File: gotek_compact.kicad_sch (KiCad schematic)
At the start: 32 parts, among them IC1 STM32F105RBT6, IC2 74AHCT08D, IC3 AP7381-33Y-13, X1 8MHz

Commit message: Updated Schematics and initial PCB placement
Schematics have been re-done based on OpenFlop from SukkoPera, with changes towards more compact design.
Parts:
- removed IC1: STM32F105RBT6, Package_QFP:LQFP-64_10x10mm_P0.5mm, symbol MCU_ST_STM32F1:STM32F105RBTx
- removed IC2: 74AHCT08D, Package_SO:SOIC-14_3.9x8.7mm_P1.27mm, symbol 74xx:74LS08
- removed IC3: AP7381-33Y-13, Package_TO_SOT_SMD:SOT-89-3, symbol Regulator_Linear:AP7381-33V
- removed LK1: BOOT0, Connector_PinHeader_2.54mm:PinHeader_1x02_P2.54mm_Vertical, symbol Connector_Generic:Conn_01x02
- removed PL1: Power 5V, Connector_PinHeader_2.54mm:PinHeader_1x02_P2.54mm_Vertical, symbol Connector_Generic:Conn_01x02
- removed PL2: Program, Connector_PinHeader_2.54mm:PinHeader_1x03_P2.54mm_Vertical, symbol Connector_Generic:Conn_01x03
- removed PL3: USB, Connector_PinHeader_2.54mm:PinHeader_1x04_P2.54mm_Vertical, symbol Connector_Generic:Conn_01x04
- removed PL5: OLED, Connector_PinHeader_2.54mm:PinHeader_1x04_P2.54mm_Vertical, symbol Connector_Generic:Conn_01x04
- removed VR1: 10K, Potentiometer_SMD:Potentiometer_Bourns_TC33X_Vertical, symbol Device:R_Potentiometer_Trim
- added C10: 100nF, Capacitor_SMD:C_0805_2012Metric, symbol Device:C
- added C11, C12: 22pF, Capacitor_SMD:C_0805_2012Metric, symbol Device:C
- added CN1: POWER_IN, gotek_compact:171826-4, symbol gotek_compact:171826-4
- added CN2: USB, gotek_compact:USB-C-SMD_GT-USB-7016, symbol gotek_compact:GT-USB-7016
- added D1: 1N4148WS, Diode_SMD:D_SOD-323, symbol Diode:1N4148WS
- added J2: USB_Prog, Connector_PinHeader_2.54mm:PinHeader_2x05_P2.54mm_Vertical, symbol Connector_Generic:Conn_02x05_Odd_Even
- added J3: OLED+SER, Connector_PinHeader_2.54mm:PinHeader_1x06_P2.54mm_Vertical, symbol Connector_Generic:Conn_01x06
- added Q1: MMBT3904, Package_TO_SOT_SMD:SOT-23, symbol Transistor_BJT:MMBT3904
- added R12: 22, Resistor_SMD:R_0805_2012Metric, symbol Device:R
- added R13: 1K, Resistor_SMD:R_0805_2012Metric, symbol Device:R
- added R14, R15: 5K1, Resistor_SMD:R_0805_2012Metric, symbol Device:R
- added R5: 4K7, Resistor_SMD:R_0805_2012Metric, symbol Device:R
- added U1: STM32F105RBT6, Package_QFP:LQFP-64_10x10mm_P0.5mm, symbol MCU_ST_STM32F1:STM32F105RBTx
- added U2: 74LCX07, Package_SO:TSSOP-14_4.4x5mm_P0.65mm, symbol 74xx:74LCX07
- added U3: AP2112K-3.3, Package_TO_SOT_SMD:SOT-23-5, symbol Regulator_Linear:AP2112K-1.2
- C1: value 10uF/16V -> 1uF; footprint Capacitor_SMD:C_1206_3216Metric -> Capacitor_SMD:C_0805_2012Metric; LCSC (none) -> C28323; Part Number (none) -> CL21B105KBFNNNE
- C2: value 100nF -> 10uF; LCSC (none) -> C15850; Part Number (none) -> CL21A106KAYNNNE
- C3: value 2u2 -> 10uF; LCSC (none) -> C15850; Part Number (none) -> CL21A106KAYNNNE
- C4, C5, C8, C9: LCSC (none) -> C49678; Part Number (none) -> CC0805KRX7R9BB104
- C6, C7: value 22pF -> 100nF; LCSC (none) -> C49678; Part Number (none) -> CC0805KRX7R9BB104
- CN3: renamed from SK1; LCSC (none) -> C601943; Part Number (none) -> 321034SG0ABK00A01
- J1: renamed from PL4; LCSC (none) -> C5383111; Part Number (none) -> 2541WV-02P
- J4: renamed from PL6; LCSC (none) -> C5383114; Part Number (none) -> 2541WV-05P
- R1, R4: LCSC (none) -> C17673; Part Number (none) -> 0805W8F4701T5E
- R10, R11, R6, R7, R8, R9: value 1K0 -> 1K; LCSC (none) -> C17513; Part Number (none) -> 0805W8F1001T5E
- R2, R3: LCSC (none) -> C17561; Part Number (none) -> 0805W8F220JT5E
- X1: footprint Crystal:Crystal_SMD_HC49-SD -> Crystal:Crystal_SMD_5032-2Pin_5.0x3.2mm; LCSC (none) -> X50328MSB2GI; Part Number (none) -> C115962
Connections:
- net SOUNDER is gone; now on net GND: R4.1
- net SOUND_POT is gone; now on net BOOT0: R4.2
- net +3V3: now also C2.1, C4.2, C5.2, C6.2, C7.2, C8.2, C9.2, R1.2, J2.10 (Pin_10), J2.7 (Pin_7), J3.4 (Pin_4), U1.1 (VBAT), U1.13 (VDDA), U1.19 (VDD), U1.32 (VDD), U1.48 (VDD), U1.64 (VDD), U2.14 (VCC), U3.5 (VOUT); no longer C4.1, C5.1, R1.1
- net +5V: now also R10.2, R11.2, R6.2, R7.2, R8.2, R9.2, CN1.1 (5V), CN2.A4B9 (VBUS), CN2.B4A9 (VBUS), J2.4 (Pin_4), R12.2, U3.1 (VIN), U3.3 (EN); no longer C2.1, C9.1, R10.1, R11.1, R6.1, R7.1, R8.1, R9.1
- net BOOT0: now also J2.9 (Pin_9), U1.60 (BOOT0)
- net ENC_CLK: now also U1.52 (PC11)
- net ENC_DT: now also U1.51 (PC10)
- net ENC_SW: now also U1.37 (PC6)
- net GND: now also C4.1, C5.1, C6.1, C7.1, C8.1, C9.1, C10.1, C11.2, C12.2, CN1.2 (GND), CN1.3 (GND), CN2.0 (SHELL), CN2.A1B12 (GND), CN2.B1A12 (GND), J2.2 (Pin_2), J2.6 (Pin_6), J2.8 (Pin_8), J3.3 (Pin_3), Q1.2 (E), R14.2, R15.2, R5.2, U1.12 (VSSA), U1.18 (VSS), U1.2 (PC13), U1.3 (PC14), U1.31 (VSS), U1.4 (PC15), U1.47 (VSS), U1.53 (PC12), U1.63 (VSS), U2.7 (GND), U3.2 (GND); no longer C4.2, C5.2, C6.2, C7.2, C8.2, C9.2, J1.2 (Pin_2)
- net NRST: now also R1.1, C10.2, J2.1 (Pin_1), U1.7 (NRST); no longer C8.1, R1.2
- net OSC_IN: now also C11.1, U1.5 (PD0); no longer C6.1
- net OSC_OUT: now also C12.1, U1.6 (PD1); no longer C7.1
- net RXD: now also J2.3 (Pin_3), U1.42 (PA9)
- net SCL: now also J3.5 (Pin_5), U1.29 (PB10)
- net SDA: now also J3.6 (Pin_6), U1.30 (PB11)
- net SOUND: now also R13.1, U1.16 (PA2); no longer J1.1 (Pin_1)
- net SWCLK: now also J3.1 (Pin_1), U1.49 (PA14)
- net SWDIO: now also J3.2 (Pin_2), U1.46 (PA13)
- net TXD: now also J2.5 (Pin_5), U1.43 (PA10)
- net _CHNG: now reaches CN3.2 (Pin_2)
- net _CHNG: now also U2.12
- net _RDY: now reaches CN3.34 (Pin_34)
- net _RDY: now also U2.10
- net DIRECTION renamed DIR
- net DIR: now also R11.1, U1.26 (PB0); no longer R11.2
- net DRIVE_SELECT_0 renamed _SEL0
- net _SEL0: now also R6.1, U1.14 (PA0); no longer R6.2
- net INDEX renamed _INDEX
- net _INDEX: now also U2.6
- net READ_DATA renamed _DKRD
- net _DKRD: now also U2.2
- net SIDE_SELECT renamed _SIDE
- net _SIDE: now also R10.1, U1.56 (PB4); no longer R10.2
- net STEP renamed _STEP
- net _STEP: now also R7.1, U1.15 (PA1); no longer R7.2
- net TRK0 renamed _TRK0
- net _TRK0: now also U2.4
- net USB_DM renamed USB_D-
- net USB_D-: now also CN2.A7 (DN1), CN2.B7 (DN2)
- net USB_DM_MCU: no longer names the net of R2.1
- net USB_DM_MCU: now also U1.44 (PA11)
- net USB_DP renamed USB_D+
- net USB_D+: now also CN2.A6 (DP1), CN2.B6 (DP2)
- net USB_DP_MCU: no longer names the net of R3.1
- net USB_DP_MCU: now also U1.45 (PA12)
- net WRITE_DATA renamed _DKWD
- net _DKWD: now also R8.1, U1.41 (PA8); no longer R8.2
- net WRITE_ENABLE renamed _DKWE
- net _DKWE: now also R9.1, U1.62 (PB9); no longer R9.2
- net WRITE_PROTECT renamed _WPROT
- net _WPROT: now also U2.8
- new net: R5.1, U1.28 (PB2)
- new net: D1.2 (A), Q1.3 (C)
- new net: Q1.1 (B), R13.2
- new net SPK+: J1.1 (Pin_1), R12.1
- new net SPK-: D1.1 (K), J1.2 (Pin_2)
- new net USB_CC1: CN2.A5 (CC1), R14.1
- new net USB_CC2: CN2.B5 (CC2), R15.1
- new net _CHNG_3V: U1.59 (PB7), U2.13
- new net _DKRD_3V: U1.23 (PA7), U2.1
- new net _INDEX_3V: U1.61 (PB8), U2.5
- new net _RDY_3V: U1.55 (PB3), U2.11
- new net _TRK0_3V: U1.58 (PB6), U2.3
- new net _WPROT_3V: U1.57 (PB5), U2.9
- no-connect marks 34 -> 28
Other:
- note added: "1K pull-ups on host-driven inputs"
- note added: "34-pin boxed IDC header (top side), standard floppy ribbon pinout"
- note added: "Open Drain Buffers to 5V TTL"
- note removed: "1K pull-ups (R6-R11) on host-driven inputs"
- note removed: "Buffers 3V3 MCU outputs to 5V TTL: Index, Track0, Write Protect, Read Data"
- note removed: "Compact Gotek core - circuit derived from CDO's Issue 1.1 design (theoddys.com) Gotek-compatible floppy emulator for the BBC Master internal 34-way floppy header. Programming: fit BOOT0 link LK1, connect 3V3 FTDI to PL2, use STM32CubeProgrammer; firmware: FlashFloppy. NOTE: Do not use with an external floppy drive connected at the same time (no open-collector drivers)."
- note removed: "PL1 -> 5V power in PL2 -> FTDI (3V3) programming PL3 -> USB-A breakout (stick) PL4 -> sound out PL5 -> 0.96in OLED (I2C) PL6 -> KY-040 style rotary encoder SK1 -> 34-pin boxed IDC, standard Shugart floppy bus"
- note removed: "SK1: 34-pin boxed IDC header (top side), standard floppy ribbon pinout"
- company: KiCad recreation of design by CDO / theoddys.com -> Derived from OpenFlops
- title: Compact Gotek / FlashFloppy core with breakout headers -> Compact Gotek / FlashFloppy with breakout headers
- moved on the sheet: CN3, J1, J4, X1

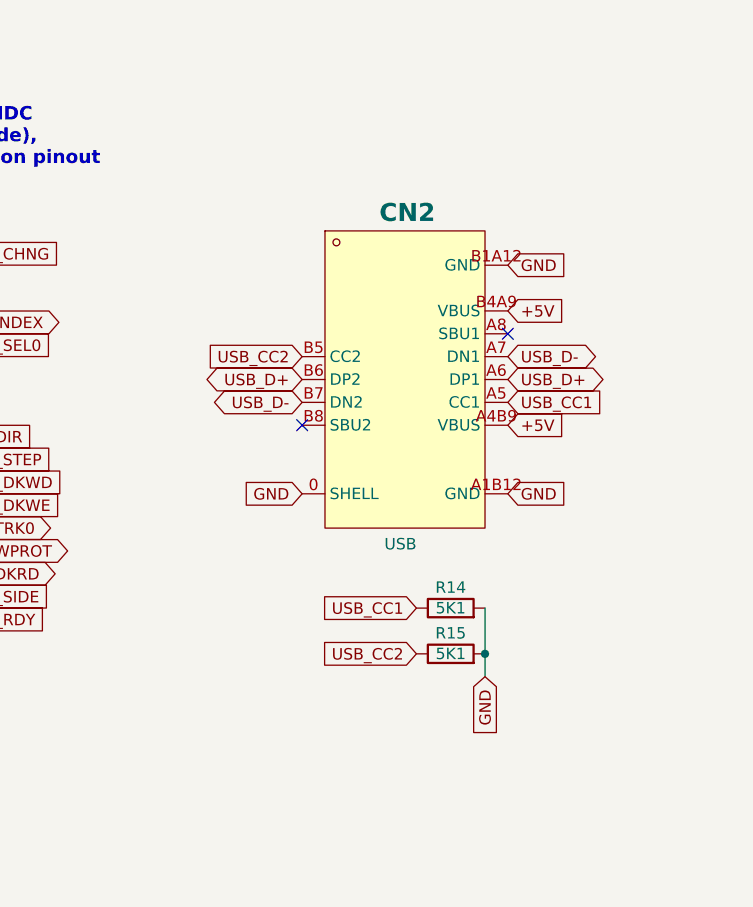
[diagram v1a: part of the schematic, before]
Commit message: USB connector changed
USB connector changed to a model without elevation
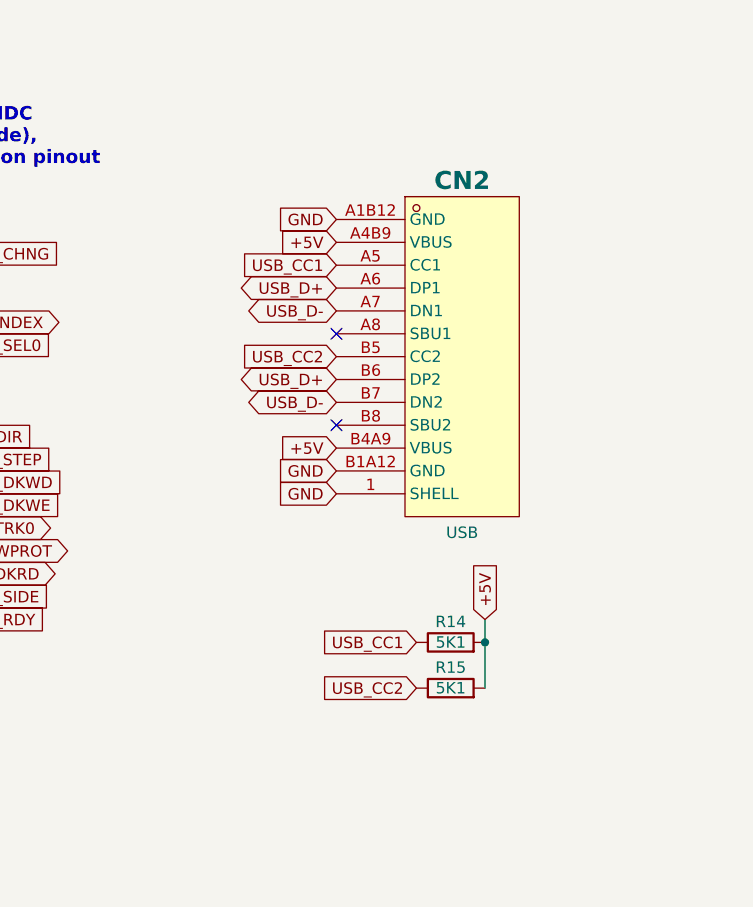
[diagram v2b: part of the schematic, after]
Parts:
- removed CN2: USB, gotek_compact:USB-C-SMD_GT-USB-7016, symbol gotek_compact:GT-USB-7016
- added CN2: USB, gotek_compact:USB-C-SMD_TYPE-C16PIN, symbol gotek_compact:TYPE-C16PIN
- U3: symbol Regulator_Linear:AP2112K-1.2 -> Regulator_Linear:AP2112K-3.3
- X1: LCSC X50328MSB2GI -> C115962; Part Number C115962 -> X50328MSB2GI
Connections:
- net +5V: now also R14.2, R15.2, CN2.A4B9 (VBUS), CN2.B4A9 (VBUS)
- net GND: now also CN2.1 (SHELL), CN2.2 (SHELL), CN2.3 (SHELL), CN2.4 (SHELL), CN2.A1B12 (GND), CN2.B1A12 (GND); no longer R14.2, R15.2
- net USB_CC1: now also CN2.A5 (CC1)
- net USB_CC2: now also CN2.B5 (CC2)
- net USB_D+: now also CN2.A6 (DP1), CN2.B6 (DP2)
- net USB_D-: now also CN2.A7 (DN1), CN2.B7 (DN2)
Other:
- moved on the sheet: R14, R15

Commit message: A few component value changes
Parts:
- C11, C12: value 22pF -> 30pF; footprint Capacitor_SMD:C_0805_2012Metric -> Capacitor_SMD:C_0603_1608Metric; LCSC C1804 -> C1658; Part Number CL21C220JBANNNC -> 0603CG300J500NT
- R14, R15: value 5K1 -> 51K; LCSC C27834 -> C17737; Part Number 0805W8F5101T5E -> 0805W8F5102T5E
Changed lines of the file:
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@@
 	)
 	(junction
+		(at 21.59 114.3)
+		(diameter 0)
+		(color 0 0 0 0)
+	)
+	(junction
 		(at 181.61 132.08)
 		(diameter 0)
@@
 	)
 	(junction
-		(at 21.59 114.3)
-		(diameter 0)
-		(color 0 0 0 0)
-	)
-	(junction
 		(at 35.56 114.3)
 		(diameter 0)
@@
 	(wire
 		(pts
+			(xy 21.59 114.3) (xy 21.59 118.11)
+		)
+		(stroke
+			(width 0)
+			(type default)
+		)
+	)
+	(wire
+		(pts
 			(xy 148.59 166.37) (xy 139.7 166.37)
 		)
@@
 	(wire
 		(pts
-			(xy 21.59 114.3) (xy 21.59 118.11)
+			(xy 21.59 105.41) (xy 21.59 114.3)
 		)
 		(stroke
@@
 	(wire
 		(pts
-			(xy 21.59 105.41) (xy 21.59 114.3)
-		)
-		(stroke
-			(width 0)
-			(type default)
-		)
-	)
-	(wire
-		(pts
 			(xy 181.61 127) (xy 181.61 129.54)
 		)
@@
 	)
 	(symbol
-		(lib_id "Device:C")
-		(at 25.4 114.3 270)
-		(unit 1)
-		(body_style 1)
-		(exclude_from_sim no)
-		(in_bom yes)
-		(on_board yes)
-		(in_pos_files yes)
-		(dnp no)
-		(property "Reference" "C12"
-			(at 26.924 113.284 90)
-			(show_name no)
-			(do_not_autoplace no)
-			(effects
-				(font
-					(size 1.27 1.27)
-				)
-				(justify left)
-			)
-		)
-		(property "Value" "22pF"
-			(at 26.924 115.824 90)
-			(show_name no)
-			(do_not_autoplace no)
-			(effects
-				(font
-					(size 1.27 1.27)
-				)
-				(justify left)
-			)
-		)
-		(property "Footprint" "Capacitor_SMD:C_0805_2012Metric"
-			(at 21.59 115.2652 0)
-			(hide yes)
-			(show_name no)
-			(do_not_autoplace no)
-			(effects
-				(font
-					(size 1.27 1.27)
-				)
-			)
-		)
-		(property "Datasheet" ""
-			(at 25.4 114.3 0)
-			(hide yes)
-			(show_name no)
-			(do_not_autoplace no)
-			(effects
-				(font
-					(size 1.27 1.27)
-				)
-			)
-		)
-		(property "Description" "Unpolarized capacitor"
-			(at 25.4 114.3 0)
-			(hide yes)
-			(show_name no)
-			(do_not_autoplace no)
-			(effects
-				(font
-					(size 1.27 1.27)
-				)
-			)
-		)
-		(property "LCSC" "C1804"
-			(at 25.4 114.3 0)
-			(hide yes)
-			(show_name no)
-			(do_not_autoplace no)
-			(effects
-				(font
-					(size 1.27 1.27)
-				)
-			)
-		)
-		(property "Part Number" "CL21C220JBANNNC"
-			(at 25.4 114.3 0)
-			(hide yes)
-			(show_name no)
-			(do_not_autoplace no)
-			(effects
-				(font
-					(size 1.27 1.27)
-				)
-			)
-		)
-		(pin "1"
-		)
-		(pin "2"
-		)
-		(instances
-			(project "gotek_compact"
-				(path "/e63e39d7-6ac0-4ffd-8aa3-1841a4541b55"
-					(reference "C12")
-					(unit 1)
-				)
-			)
-		)
-	)
-	(symbol
 		(lib_id "Device:R")
 		(at 248.92 152.4 90)
@@
 			)
 		)
-		(property "Value" "5K1"
+		(property "Value" "51K"
 			(at 248.92 152.4 90)
 			(show_name no)
@@
 			)
 		)
-		(property "LCSC" "C27834"
+		(property "LCSC" "C17737"
 			(at 248.92 152.4 90)
 			(hide yes)
@@
 			)
 		)
-		(property "Part Number" "0805W8F5101T5E"
+		(property "Part Number" "0805W8F5102T5E"
 			(at 248.92 152.4 90)
 			(hide yes)
@@
 			)
 		)
-		(property "Value" "22pF"
+		(property "Value" "30pF"
 			(at 27.178 106.934 90)
 			(show_name no)
@@
 			)
 		)
-		(property "Footprint" "Capacitor_SMD:C_0805_2012Metric"
+		(property "Footprint" "Capacitor_SMD:C_0603_1608Metric"
 			(at 21.59 106.3752 0)
 			(hide yes)
@@
 			)
 		)
-		(property "LCSC" "C1804"
+		(property "LCSC" "C1658"
 			(at 25.4 105.41 0)
 			(hide yes)
@@
 			)
 		)
-		(property "Part Number" "CL21C220JBANNNC"
+		(property "Part Number" "0603CG300J500NT"
 			(at 25.4 105.41 0)
 			(hide yes)
@@
 	)
 	(symbol
+		(lib_id "Device:C")
+		(at 25.4 114.3 270)
+		(unit 1)
+		(body_style 1)
+		(exclude_from_sim no)
+		(in_bom yes)
+		(on_board yes)
+		(in_pos_files yes)
+		(dnp no)
+		(property "Reference" "C12"
+			(at 26.924 113.284 90)
+			(show_name no)
+			(do_not_autoplace no)
+			(effects
+				(font
+					(size 1.27 1.27)
+				)
+				(justify left)
+			)
+		)
+		(property "Value" "30pF"
+			(at 27.178 115.824 90)
+			(show_name no)
+			(do_not_autoplace no)
+			(effects
+				(font
+					(size 1.27 1.27)
+				)
+				(justify left)
+			)
+		)
+		(property "Footprint" "Capacitor_SMD:C_0603_1608Metric"
+			(at 21.59 115.2652 0)
+			(hide yes)
+			(show_name no)
+			(do_not_autoplace no)
+			(effects
+				(font
+					(size 1.27 1.27)
+				)
+			)
+		)
+		(property "Datasheet" ""
+			(at 25.4 114.3 0)
+			(hide yes)
+			(show_name no)
+			(do_not_autoplace no)
+			(effects
+				(font
+					(size 1.27 1.27)
+				)
+			)
+		)
+		(property "Description" "Unpolarized capacitor"
+			(at 25.4 114.3 0)
+			(hide yes)
+			(show_name no)
+			(do_not_autoplace no)
+			(effects
+				(font
+					(size 1.27 1.27)
+				)
+			)
+		)
+		(property "LCSC" "C1658"
+			(at 25.4 114.3 0)
+			(hide yes)
+			(show_name no)
+			(do_not_autoplace no)
+			(effects
+				(font
+					(size 1.27 1.27)
+				)
+			)
+		)
+		(property "Part Number" "0603CG300J500NT"
+			(at 25.4 114.3 0)
+			(hide yes)
+			(show_name no)
+			(do_not_autoplace no)
+			(effects
+				(font
+					(size 1.27 1.27)
+				)
+			)
+		)
+		(pin "1"
+		)
+		(pin "2"
+		)
+		(instances
+			(project "gotek_compact"
+				(path "/e63e39d7-6ac0-4ffd-8aa3-1841a4541b55"
+					(reference "C12")
+					(unit 1)
+				)
+			)
+		)
+	)
+	(symbol
 		(lib_id "74xx:74LCX07")
 		(at 139.7 104.14 0)
@@
 			)
 		)
-		(property "Value" "5K1"
+		(property "Value" "51K"
 			(at 248.92 147.32 90)
 			(show_name no)
@@
 			)
 		)
-		(property "LCSC" "C27834"
+		(property "LCSC" "C17737"
 			(at 248.92 147.32 90)
 			(hide yes)
@@
 			)
 		)
-		(property "Part Number" "0805W8F5101T5E"
+		(property "Part Number" "0805W8F5102T5E"
 			(at 248.92 147.32 90)
 			(hide yes)

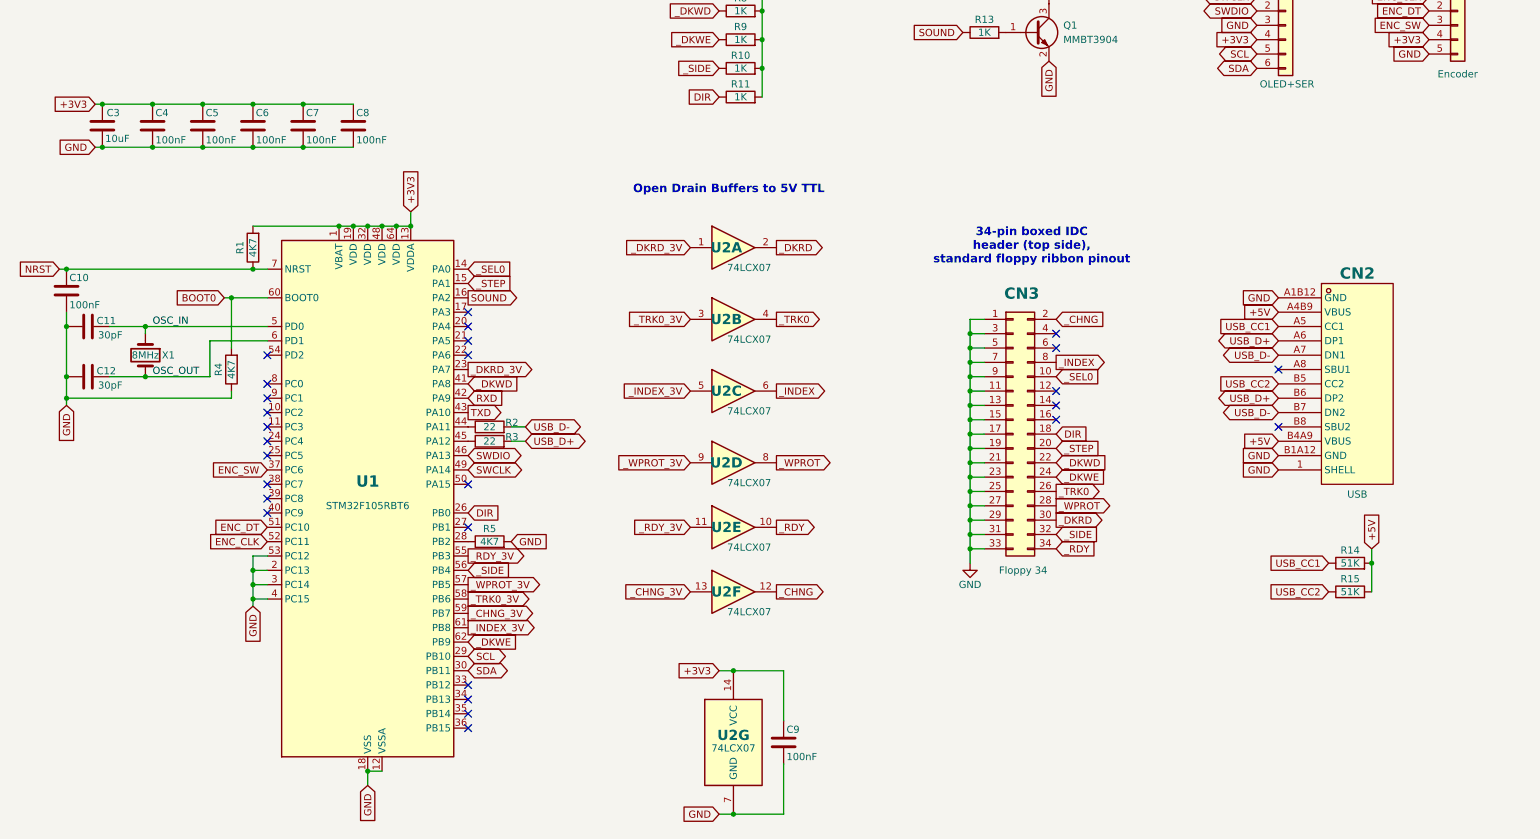
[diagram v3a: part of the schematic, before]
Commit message: PCB routing finished
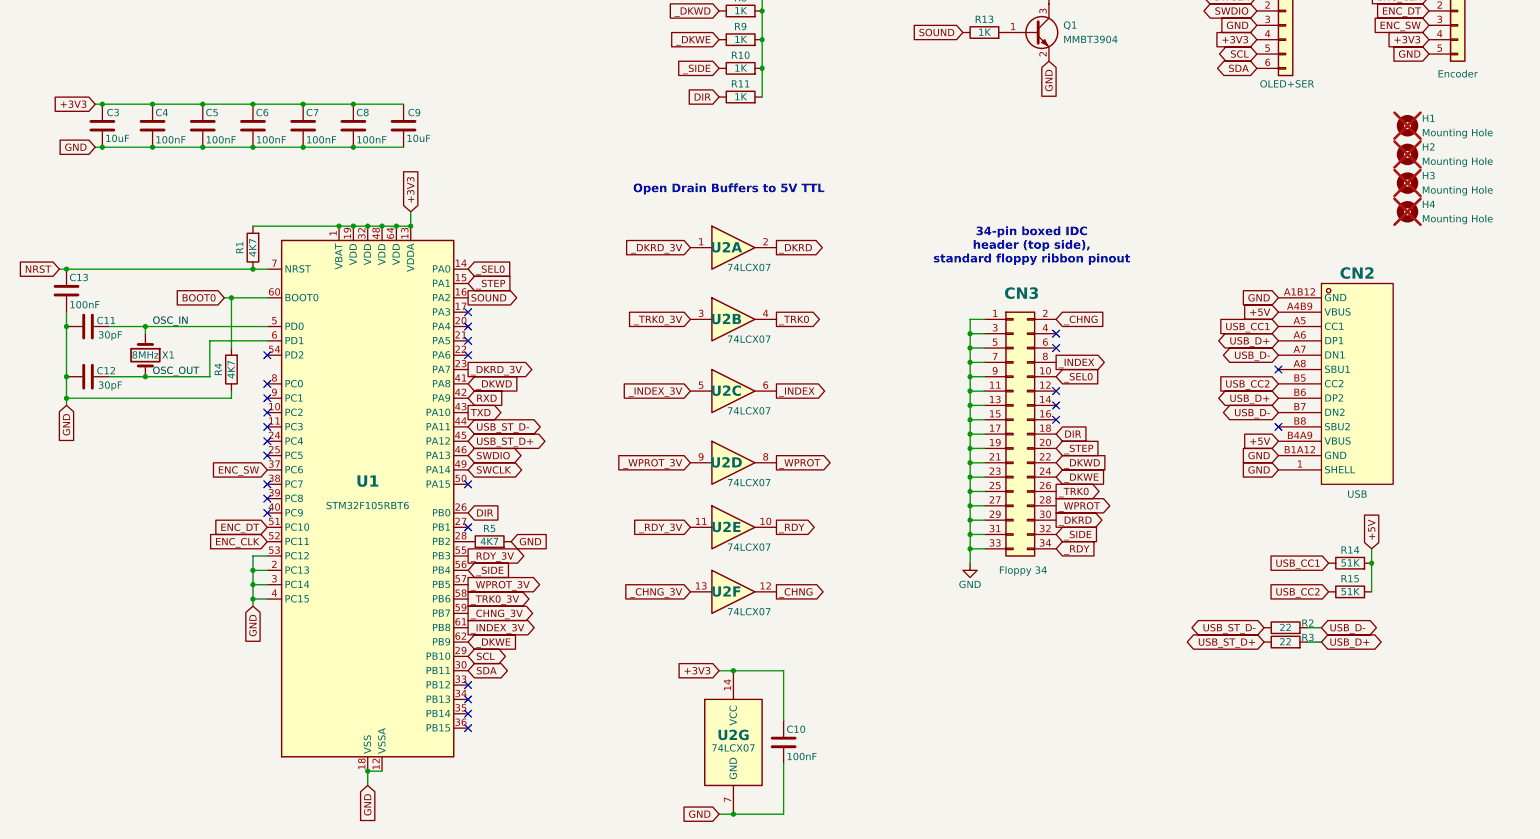
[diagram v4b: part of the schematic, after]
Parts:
- added C9: 10uF, Capacitor_SMD:C_0805_2012Metric, symbol Device:C
- added H1, H2, H3, H4: Mounting Hole, MountingHole:MountingHole_2.7mm_M2.5, symbol Mechanical:MountingHole
- renumbered C9 to C10, C10 to C13
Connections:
- net +3V3: now also C9.1
- net GND: now also C9.2
- net USB_ST_D-: now reaches R2.1, U1.44 (PA11)
- net USB_ST_D+: now reaches R3.1, U1.45 (PA12)
